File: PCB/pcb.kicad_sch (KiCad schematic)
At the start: 9 parts, among them SW1 SW_Push, SW2 SW_Push, SW3 SW_Push, SW4 SW_Push, SW5 SW_Push, SW6 SW_Push, U1 XIAO-RP2040-DIP

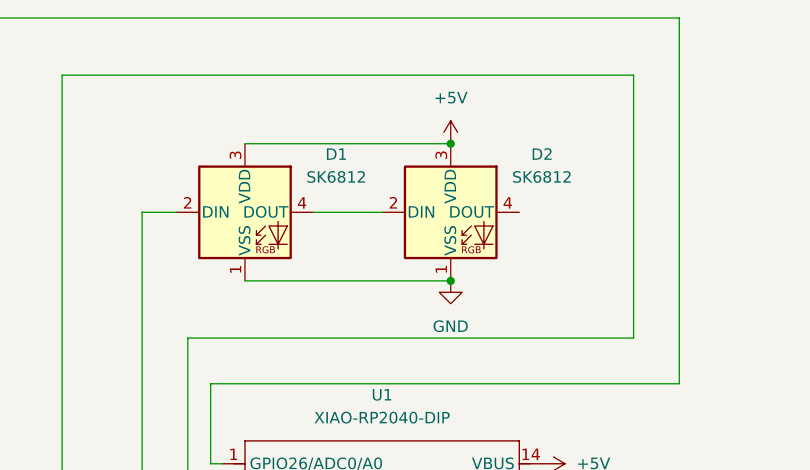
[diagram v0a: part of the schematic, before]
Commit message: Changed from SK6812 to SK6812MINI-E
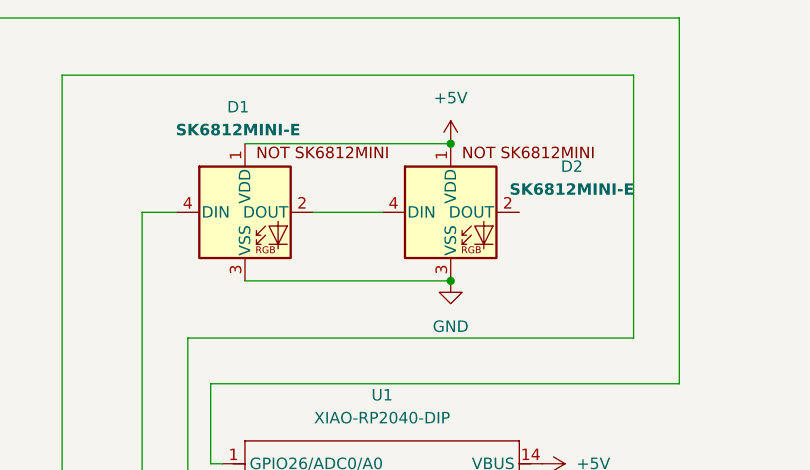
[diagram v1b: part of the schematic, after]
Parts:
- removed D1, D2: SK6812, LED_SMD:LED_SK6812MINI_PLCC4_3.5x3.5mm_P1.75mm, symbol LED:SK6812
- added D1, D2: SK6812MINI-E, Hackclub Footprints:MX_SK6812MINI-E_REV, symbol HACKCLUB_SYM:SK6812MINI-E
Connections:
- net +5V: now also D1.1 (VDD), D2.1 (VDD)
- net GND: now also D1.3 (VSS), D2.3 (VSS)
- net at U1.5 (GPIO6/SDA): now also D1.4 (DIN)
- new net: D1.2 (DOUT), D2.4 (DIN)
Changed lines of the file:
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@@
 	(paper "A4")
-	(junction
-		(at 140.97 34.29)
-		(diameter 0)
-		(color 0 0 0 0)
-	)
 	(junction
 		(at 58.42 71.12)
@@
 	)
 	(junction
-		(at 140.97 49.53)
-		(diameter 0)
-		(color 0 0 0 0)
-	)
-	(junction
 		(at 58.42 106.68)
 		(diameter 0)
@@
 	)
 	(junction
+		(at 140.97 49.53)
+		(diameter 0)
+		(color 0 0 0 0)
+	)
+	(junction
 		(at 58.42 144.78)
+		(diameter 0)
+		(color 0 0 0 0)
+	)
+	(junction
+		(at 140.97 34.29)
 		(diameter 0)
 		(color 0 0 0 0)
@@
 	)
 	(symbol
+		(lib_id "HACKCLUB_SYM:SK6812MINI-E")
+		(at 118.11 41.91 0)
+		(unit 1)
+		(exclude_from_sim no)
+		(in_bom yes)
+		(on_board yes)
+		(dnp no)
+		(property "Reference" "D1"
+			(at 117.348 30.2259 0)
+			(effects
+				(font
+					(size 1.27 1.27)
+				)
+			)
+		)
+		(property "Value" "SK6812MINI-E"
+			(at 117.348 32.766 0)
+			(effects
+				(font
+					(size 1.27 1.27)
+					(thickness 0.254)
+					(bold yes)
+				)
+			)
+		)
+		(property "Footprint" "Hackclub Footprints:MX_SK6812MINI-E_REV"
+			(at 119.38 49.53 0)
+			(effects
+				(font
+					(size 1.27 1.27)
+				)
+				(justify left top)
+				(hide yes)
+			)
+		)
+		(property "Datasheet" "https://cdn-shop.adafruit.com/product-files/4960/4960_SK6812MINI-E_REV02_EN.pdf"
+			(at 120.65 51.435 0)
+			(effects
+				(font
+					(size 1.27 1.27)
+				)
+				(justify left top)
+				(hide yes)
+			)
+		)
+		(property "Description" "RGB LED with integrated controller"
+			(at 118.11 41.91 0)
+			(effects
+				(font
+					(size 1.27 1.27)
+				)
+				(hide yes)
+			)
+		)
+		(pin "2"
+		)
+		(pin "1"
+		)
+		(pin "4"
+		)
+		(pin "3"
+		)
+		(instances
+			(project ""
+				(path "/ba72bc38-65c9-43dc-b1da-21c24f79285e"
+					(reference "D1")
+					(unit 1)
+				)
+			)
+		)
+	)
+	(symbol
+		(lib_id "HACKCLUB_SYM:SK6812MINI-E")
+		(at 140.97 41.91 0)
+		(unit 1)
+		(exclude_from_sim no)
+		(in_bom yes)
+		(on_board yes)
+		(dnp no)
+		(property "Reference" "D2"
+			(at 154.432 36.8299 0)
+			(effects
+				(font
+					(size 1.27 1.27)
+				)
+			)
+		)
+		(property "Value" "SK6812MINI-E"
+			(at 154.432 39.37 0)
+			(effects
+				(font
+					(size 1.27 1.27)
+					(thickness 0.254)
+					(bold yes)
+				)
+			)
+		)
+		(property "Footprint" "Hackclub Footprints:MX_SK6812MINI-E_REV"
+			(at 142.24 49.53 0)
+			(effects
+				(font
+					(size 1.27 1.27)
+				)
+				(justify left top)
+				(hide yes)
+			)
+		)
+		(property "Datasheet" "https://cdn-shop.adafruit.com/product-files/4960/4960_SK6812MINI-E_REV02_EN.pdf"
+			(at 143.51 51.435 0)
+			(effects
+				(font
+					(size 1.27 1.27)
+				)
+				(justify left top)
+				(hide yes)
+			)
+		)
+		(property "Description" "RGB LED with integrated controller"
+			(at 140.97 41.91 0)
+			(effects
+				(font
+					(size 1.27 1.27)
+				)
+				(hide yes)
+			)
+		)
+		(pin "2"
+		)
+		(pin "1"
+		)
+		(pin "4"
+		)
+		(pin "3"
+		)
+		(instances
+			(project ""
+				(path "/ba72bc38-65c9-43dc-b1da-21c24f79285e"
+					(reference "D2")
+					(unit 1)
+				)
+			)
+		)
+	)
+	(symbol
 		(lib_id "Switch:SW_Push")
 		(at 63.5 48.26 0)
@@
 	)
 	(symbol
-		(lib_id "LED:SK6812")
-		(at 118.11 41.91 0)
-		(unit 1)
-		(exclude_from_sim no)
-		(in_bom yes)
-		(on_board yes)
-		(dnp no)
-		(fields_autoplaced yes)
-		(property "Reference" "D1"
-			(at 128.27 35.4898 0)
-			(effects
-				(font
-					(size 1.27 1.27)
-				)
-			)
-		)
-		(property "Value" "SK6812"
-			(at 128.27 38.0298 0)
-			(effects
-				(font
-					(size 1.27 1.27)
-				)
-			)
-		)
-		(property "Footprint" "LED_SMD:LED_SK6812MINI_PLCC4_3.5x3.5mm_P1.75mm"
-			(at 119.38 49.53 0)
-			(effects
-				(font
-					(size 1.27 1.27)
-				)
-				(justify left top)
-				(hide yes)
-			)
-		)
-		(property "Datasheet" "https://cdn-shop.adafruit.com/product-files/1138/SK6812+LED+datasheet+.pdf"
-			(at 120.65 51.435 0)
-			(effects
-				(font
-					(size 1.27 1.27)
-				)
-				(justify left top)
-				(hide yes)
-			)
-		)
-		(property "Description" "RGB LED with integrated controller"
-			(at 118.11 41.91 0)
-			(effects
-				(font
-					(size 1.27 1.27)
-				)
-				(hide yes)
-			)
-		)
-		(pin "3"
-		)
-		(pin "2"
-		)
-		(pin "4"
-		)
-		(pin "1"
-		)
-		(instances
-			(project ""
-				(path "/ba72bc38-65c9-43dc-b1da-21c24f79285e"
-					(reference "D1")
-					(unit 1)
-				)
-			)
-		)
-	)
-	(symbol
 		(lib_id "power:GND")
 		(at 151.13 73.66 90)
@@
 					(unit 1)
 				)
-			)
-		)
-	)
-	(symbol
-		(lib_id "LED:SK6812")
-		(at 140.97 41.91 0)
-		(unit 1)
-		(exclude_from_sim no)
-		(in_bom yes)
-		(on_board yes)
-		(dnp no)
-		(fields_autoplaced yes)
-		(property "Reference" "D2"
-			(at 151.13 35.4898 0)
-			(effects
-				(font
-					(size 1.27 1.27)
-				)
-			)
-		)
-		(property "Value" "SK6812"
-			(at 151.13 38.0298 0)
-			(effects
-				(font
-					(size 1.27 1.27)
-				)
-			)
-		)
-		(property "Footprint" "LED_SMD:LED_SK6812MINI_PLCC4_3.5x3.5mm_P1.75mm"
-			(at 142.24 49.53 0)
-			(effects
-				(font
-					(size 1.27 1.27)
-				)
-				(justify left top)
-				(hide yes)
-			)
-		)
-		(property "Datasheet" "https://cdn-shop.adafruit.com/product-files/1138/SK6812+LED+datasheet+.pdf"
-			(at 143.51 51.435 0)
-			(effects
-				(font
-					(size 1.27 1.27)
-				)
-				(justify left top)
-				(hide yes)
-			)
-		)
-		(property "Description" "RGB LED with integrated controller"
-			(at 140.97 41.91 0)
-			(effects
-				(font
-					(size 1.27 1.27)
-				)
-				(hide yes)
-			)
-		)
-		(pin "3"
-		)
-		(pin "2"
-		)
-		(pin "4"
-		)
-		(pin "1"
-		)
-		(instances
-			(project ""
-				(path "/ba72bc38-65c9-43dc-b1da-21c24f79285e"
-					(reference "D2")
-					(unit 1)
-				)
